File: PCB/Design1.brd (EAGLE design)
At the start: 73 x 41 mm, 39 parts, among them J1 FTDI_DEVICE, U1 ATMEGA2560AU, Y1 16MHZ

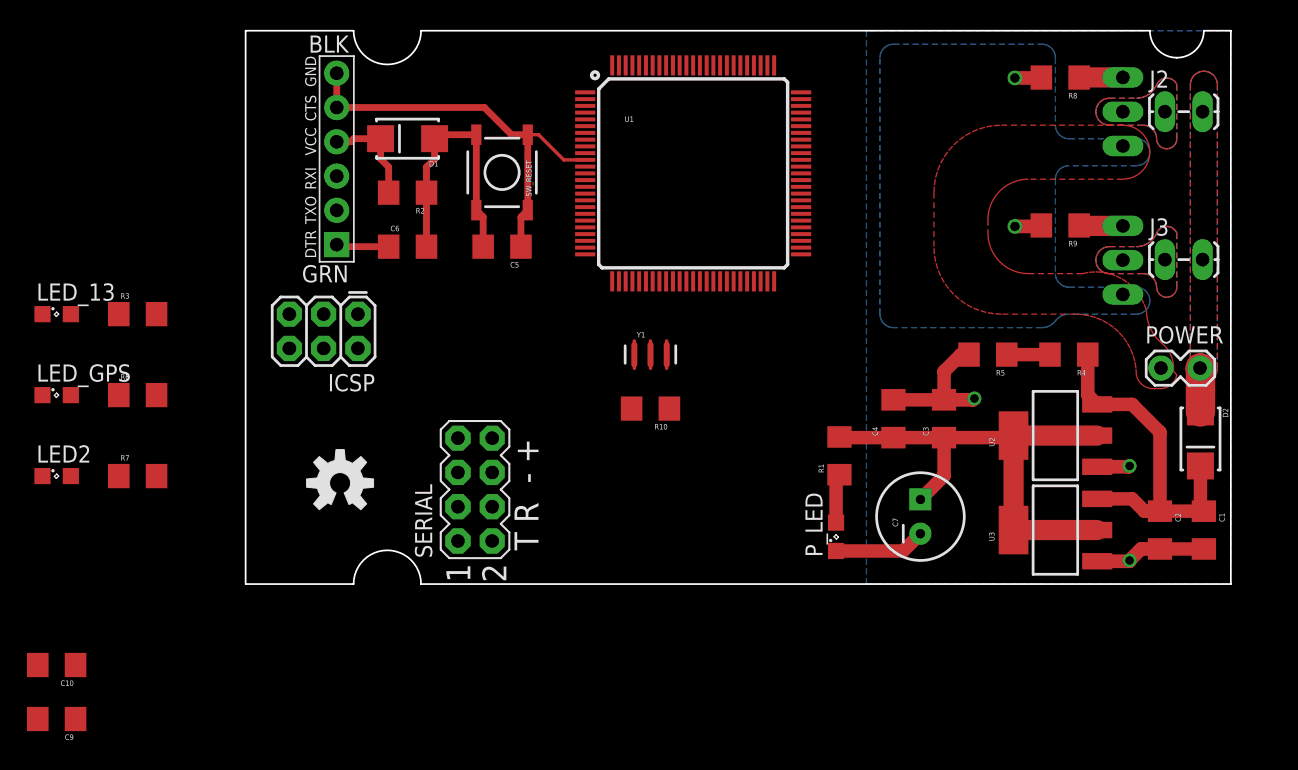
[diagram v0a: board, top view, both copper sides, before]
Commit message: Finalize part locations; Route most of the traces
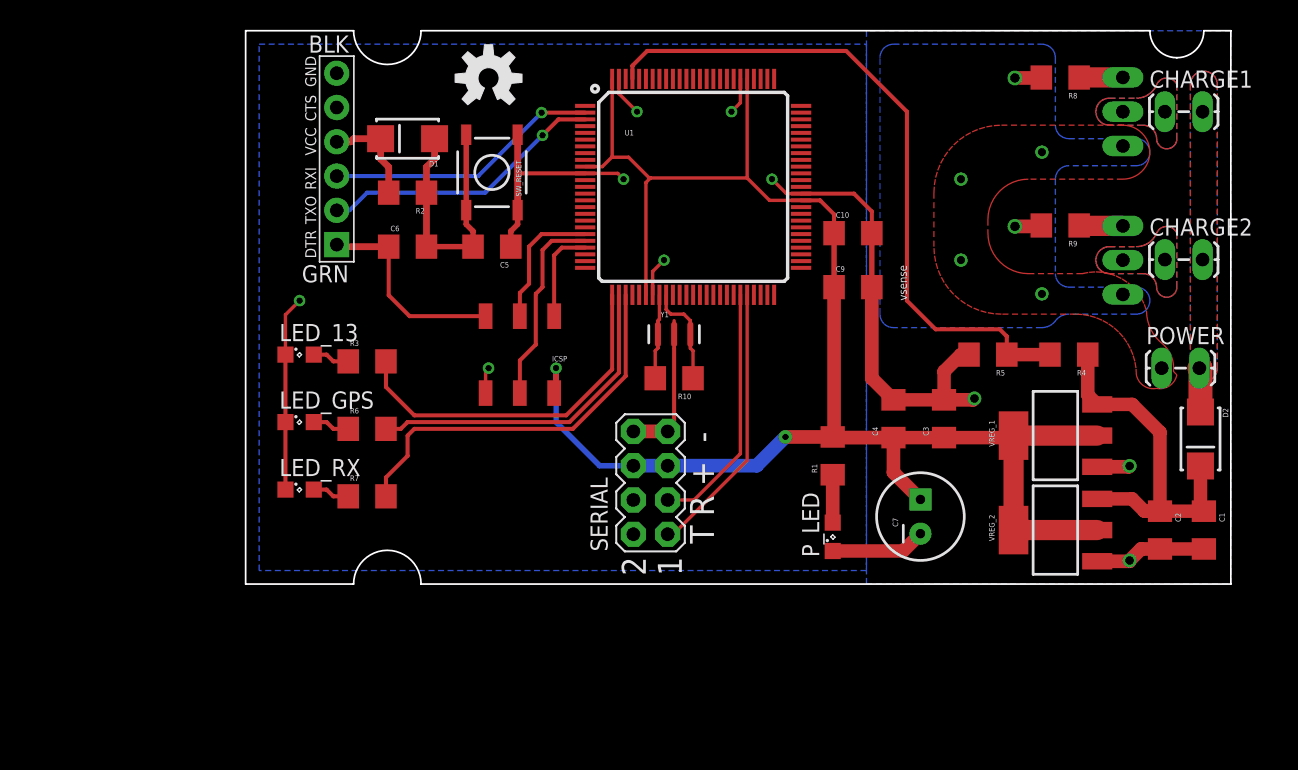
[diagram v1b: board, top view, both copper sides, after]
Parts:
- removed LED2: green, led:SML0805
- added LED_RX: green, led:SML0805
- ICSP: device SparkFun-Connectors:2X3 -> SparkFun-Connectors:2X3_SMD
- POWER: device SparkFun-Connectors:1X02_LOCK -> SparkFun-Connectors:1X02_LOCK_LONGPADS
- moved C10 67.1 mm to (45.0, 26.0), turned to 0 degrees
- moved C9 67.1 mm to (45.0, 22.0), turned to 0 degrees
- moved LOGO1 32.0 mm to (18.0, 37.5)
- moved LED_13 18.2 mm to (4.00, 17.0)
- moved LED_GPS 18.1 mm to (4.00, 12.0)
- moved R3 17.4 mm to (9.00, 16.5)
- moved R6 17.2 mm to (9.00, 11.5)
- moved R7 17.1 mm to (9.00, 6.50)
- moved SERIAL 13.0 mm to (30.0, 7.50)
- moved ICSP 12.4 mm to (20.3, 17.0)
- moved R10 2.85 mm to (31.8, 15.2)
- moved Y1 2.30 mm to (31.8, 18.5)
- moved U1 1.00 mm to (33.2, 29.4)
- moved C5 0.75 mm to (18.2, 25.0)
- moved SW_RESET 0.75 mm to (18.2, 30.5)
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- renumbered J2 to CHARGE1, J3 to CHARGE2, U2 to VREG_1, U3 to VREG_2
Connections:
- removed net LED_: R7.2
- new net LED_RX: R7.2, U1.28
- net 5V: now also SERIAL.5, SERIAL.6; no longer SERIAL.7, SERIAL.8
- net GND: now also LED_RX.C, SERIAL.7, SERIAL.8; no longer LED2.C, SERIAL.5, SERIAL.6
- net LED_GPS: now also U1.27
- net N$4: now also LED_RX.A; no longer LED2.A
- net RX1: now also SERIAL.3; no longer SERIAL.4
- net RX2: now also SERIAL.4; no longer SERIAL.3
- net TX1: now also SERIAL.1; no longer SERIAL.2
- net TX2: now also SERIAL.2; no longer SERIAL.1
- net VSENSE: now also U1.97
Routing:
- net 5V: track 45.3 -> 133.5 mm, vias 0 -> 2
- net VSENSE: track 3.20 -> 50.7 mm
- net GND: track 63.1 -> 106.2 mm, vias 5 -> 16
- net LED_RX: track 0.00 -> 29.2 mm
- net LED_13: track 0.00 -> 26.5 mm
- net LED_GPS: track 0.00 -> 24.8 mm
- net TX0: track 0.00 -> 21.2 mm, vias 0 -> 1
- net TX1: track 0.00 -> 20.4 mm
- net RX0: track 0.00 -> 20.4 mm, vias 0 -> 1
- net RX1: track 0.00 -> 18.6 mm
- net MOSI: track 0.00 -> 14.7 mm
- net DTR: track 3.91 -> 15.3 mm
- net SCK: track 0.00 -> 9.98 mm
- net MISO: track 0.00 -> 7.05 mm
- net XTAL1: track 0.00 -> 5.54 mm
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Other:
- board text added: "2 1"
- board text added: "T R + -"
- board text added: "vsense"
- board text removed: "1 2"
- board text removed: "T R - +"

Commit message: Finish routing traces
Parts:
- moved LOGO1 0.71 mm to (17.5, 37.0)
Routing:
- net TX2: track 0.00 -> 32.8 mm, vias 0 -> 1
- net RX2: track 0.00 -> 30.3 mm, vias 0 -> 1
- net 5V: track 133.5 -> 155.3 mm
- net GND: track 106.2 -> 103.6 mm
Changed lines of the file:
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@@
 <text x="32.32" y="0.62" size="1.778" layer="21" rot="R90">2
 1</text>
-<dimension x1="75" y1="41" x2="75" y2="0" x3="78.943428125" y3="20.5" textsize="1.778" layer="51" visible="yes"/>
+<dimension x1="74" y1="41" x2="74" y2="0" x3="78.92931875" y3="20.5" textsize="1.778" layer="51" visible="yes"/>
 <dimension x1="0" y1="42" x2="73" y2="42" x3="36.5" y3="45" textsize="1.778" layer="51" visible="yes"/>
 <wire x1="46" y1="41" x2="46" y2="18" width="0.254" layer="22"/>
@@
 <element name="J1" library="SparkFun-Connectors" package="FTDI_DEVICE_SIDE" value="FTDI_DEVICE" x="6.75" y="31.5" locked="yes" rot="R90"/>
 <element name="D1" library="SparkFun-DiscreteSemi" package="SMA-DIODE_ALT" value="" x="12" y="33" rot="R180"/>
-<element name="LOGO1" library="SparkFun-Aesthetics" package="OSHW-LOGO-M" value="OSHW-LOGOM" x="18" y="37.48"/>
+<element name="LOGO1" library="SparkFun-Aesthetics" package="OSHW-LOGO-M" value="OSHW-LOGOM" x="17.5" y="36.98"/>
 <element name="LED_13" library="led" package="SML0805" value="blue" x="4" y="17"/>
 <element name="POWER" library="SparkFun-Connectors" package="1X02_LOCK_LONGPADS" value="" x="68" y="16" locked="yes"/>
@@
 <contactref element="SERIAL" pad="7"/>
 <contactref element="SERIAL" pad="8"/>
-<wire x1="31.27" y1="11.31" x2="28.73" y2="11.31" width="1.016" layer="1"/>
 <wire x1="31.75" y1="17.484" x2="31.75" y2="11.79" width="0.3048" layer="1"/>
 <wire x1="31.75" y1="11.79" x2="31.27" y2="11.31" width="0.3048" layer="1"/>
@@
 <wire x1="6.75" y1="25.15" x2="6.9" y2="25" width="0.508" layer="1"/>
 <wire x1="6.9" y1="25" x2="10.6" y2="25" width="0.508" layer="1"/>
-<wire x1="10.6" y1="25" x2="10.6" y2="21.4" width="0.3" layer="1"/>
-<wire x1="10.6" y1="21.4" x2="12.15" y2="19.85" width="0.3" layer="1"/>
-<wire x1="12.15" y1="19.85" x2="17.78" y2="19.85" width="0.3" layer="1"/>
+<wire x1="17.78" y1="19.85" x2="17.78" y2="21.47" width="0.3" layer="1"/>
+<wire x1="17" y1="22.25" x2="11.25" y2="22.25" width="0.3" layer="1"/>
+<wire x1="10.6" y1="22.9" x2="10.6" y2="25" width="0.3" layer="1"/>
+<wire x1="10.6" y1="22.9" x2="11.25" y2="22.25" width="0.3" layer="1"/>
+<wire x1="17.78" y1="21.47" x2="17" y2="22.25" width="0.3" layer="1"/>
 </signal>
 <signal name="LED_13">
@@
 <wire x1="43.6" y1="27.4" x2="43.6" y2="26" width="0.3" layer="1"/>
 <wire x1="43.6" y1="26" x2="43.6" y2="22" width="0.4064" layer="1"/>
-<wire x1="27.16" y1="37.43" x2="27.16" y2="31.66" width="0.254" layer="1"/>
 <wire x1="27.16" y1="31.66" x2="27.125" y2="31.625" width="0.254" layer="1"/>
 <wire x1="27.125" y1="31.625" x2="26.43" y2="30.93" width="0.254" layer="1"/>
@@
 <wire x1="23" y1="16" x2="23" y2="14.29" width="0.4064" layer="1"/>
 <wire x1="23" y1="14.29" x2="22.86" y2="14.15" width="0.4064" layer="1"/>
-<wire x1="25.16" y1="30.93" x2="10.6" y2="30.9" width="0" layer="19" extent="1-1"/>
+<wire x1="27.16" y1="31.66" x2="27.16" y2="37.43" width="0.254" layer="1"/>
+<wire x1="27.16" y1="37.43" x2="27.16" y2="38.34" width="0.3" layer="1"/>
+<wire x1="27.16" y1="38.34" x2="26.75" y2="38.75" width="0.3" layer="1"/>
+<wire x1="26.75" y1="38.75" x2="13.75" y2="38.75" width="0.3" layer="1"/>
+<wire x1="13.75" y1="38.75" x2="10" y2="35" width="0.3" layer="1"/>
+<wire x1="10" y1="35" x2="10" y2="33" width="0.3" layer="1"/>
 </signal>
 <signal name="TX1">
@@
 <contactref element="U1" pad="13"/>
 <contactref element="SERIAL" pad="2"/>
-<wire x1="28.73" y1="3.69" x2="25.16" y2="29.43" width="0" layer="19" extent="1-1"/>
+<wire x1="28.73" y1="3.69" x2="20.75" y2="11.67" width="0.3" layer="16"/>
+<wire x1="20.75" y1="11.67" x2="20.75" y2="28.25" width="0.3" layer="16"/>
+<wire x1="25.16" y1="29.43" x2="23.43" y2="29.43" width="0.3" layer="1"/>
+<wire x1="23.43" y1="29.43" x2="23" y2="29" width="0.3" layer="1"/>
+<via x="23" y="29" extent="1-16" drill="0.4572"/>
+<wire x1="23" y1="29" x2="21.5" y2="29" width="0.3" layer="16"/>
+<wire x1="21.5" y1="29" x2="20.75" y2="28.25" width="0.3" layer="16"/>
 </signal>
 <signal name="RX2">
 <contactref element="U1" pad="12"/>
 <contactref element="SERIAL" pad="4"/>
-<wire x1="28.73" y1="6.23" x2="25.16" y2="29.93" width="0" layer="19" extent="1-1"/>
+<wire x1="28.73" y1="6.23" x2="27.52" y2="6.23" width="0.3" layer="16"/>
+<wire x1="27.52" y1="6.23" x2="21.75" y2="12" width="0.3" layer="16"/>
+<wire x1="21.75" y1="12" x2="21.75" y2="27.75" width="0.3" layer="16"/>
+<wire x1="25.16" y1="29.93" x2="22.43" y2="29.93" width="0.3" layer="1"/>
+<wire x1="22.43" y1="29.93" x2="21.75" y2="29.25" width="0.3" layer="1"/>
+<wire x1="21.75" y1="29.25" x2="21.75" y2="27.75" width="0.3" layer="1"/>
+<via x="21.75" y="27.75" extent="1-16" drill="0.4572"/>
 </signal>
 <signal name="VIN">

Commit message: minor fixes
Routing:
- net RESET: track 20.6 -> 41.8 mm, vias 0 -> 2
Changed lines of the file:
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@@
 <text x="32.32" y="0.62" size="1.778" layer="21" rot="R90">2
 1</text>
-<dimension x1="74" y1="41" x2="74" y2="0" x3="78.92931875" y3="20.5" textsize="1.778" layer="51" visible="yes"/>
-<dimension x1="0" y1="42" x2="73" y2="42" x3="36.5" y3="45" textsize="1.778" layer="51" visible="yes"/>
+<dimension x1="74" y1="41" x2="74" y2="0" x3="78" y3="20.5" textsize="1.778" layer="51" visible="yes"/>
+<dimension x1="0" y1="42" x2="73" y2="42" x3="36.5" y3="43" textsize="1.778" layer="51" visible="yes"/>
 <wire x1="46" y1="41" x2="46" y2="18" width="0.254" layer="22"/>
 <wire x1="46" y1="18" x2="65" y2="18" width="0.254" layer="22"/>
@@
 <wire x1="16.85" y1="25" x2="13.4" y2="25" width="0.4064" layer="1"/>
 <wire x1="16.345" y1="33.294" x2="16.345" y2="27.706" width="0.4064" layer="1"/>
-<wire x1="16.85" y1="25" x2="29.16" y2="21.43" width="0" layer="19" extent="1-1"/>
+<wire x1="16.85" y1="25" x2="16.85" y2="25.85" width="0.3" layer="1"/>
+<wire x1="16.85" y1="25.85" x2="18" y2="27" width="0.3" layer="1"/>
+<via x="18" y="27" extent="1-16" drill="0.4572"/>
+<wire x1="18" y1="27" x2="21.5" y2="30.5" width="0.3" layer="16"/>
+<wire x1="21.5" y1="30.5" x2="24" y2="30.5" width="0.3" layer="16"/>
+<wire x1="24" y1="30.5" x2="28" y2="26.5" width="0.3" layer="16"/>
+<wire x1="28" y1="26.5" x2="28" y2="25" width="0.3" layer="16"/>
+<via x="28" y="25" extent="1-16" drill="0.4572"/>
+<wire x1="28" y1="25" x2="29.16" y2="23.84" width="0.3" layer="1"/>
+<wire x1="29.16" y1="23.84" x2="29.16" y2="21.43" width="0.3" layer="1"/>
 </signal>
 <signal name="DTR">
